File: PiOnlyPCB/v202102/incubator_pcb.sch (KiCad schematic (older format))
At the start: 34 parts, among them J1 Conn_01x04, J10 Conn_01x02, J11 Conn_01x02, J2 Conn_01x04, J3 Conn_01x04, J4 Conn_01x02, J5 Conn_01x02, J6 Conn_01x02, J7 Conn_01x02, J8 Conn_01x02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

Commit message: Partial version with GPIO expander too.
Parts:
- removed D1, D2: LED, Diode_SMD:D_0805_2012Metric_Pad1.15x1.40mm_HandSolder, symbol Device:LED
- removed J1, J2, J3: Conn_01x04, Connector_PinHeader_2.54mm:PinHeader_1x04_P2.54mm_Vertical, symbol Connector_Generic:Conn_01x04
- removed J10, J11, J4, J5, J6, J7, J8, J9: Conn_01x02, TerminalBlock_Phoenix:TerminalBlock_Phoenix_MKDS-1,5-2_1x02_P5.00mm_Horizontal, symbol Connector_Generic:Conn_01x02
- removed Q1, Q2, Q3, Q4: Q_NMOS_GDS, Package_TO_SOT_THT:TO-220-3_Vertical, symbol Device:Q_NMOS_GDS
- removed R10, R11, R12, R13, R14, R15, R2, R3, R4, R5, R6, R7, R8, R9: R_Small, Resistor_SMD:R_0805_2012Metric_Pad1.15x1.40mm_HandSolder, symbol Device:R_Small
- added J1: Conn_01x05, Connector_PinHeader_2.54mm:PinHeader_1x05_P2.54mm_Vertical, symbol Connector_Generic:Conn_01x05
- added J2: Conn_01x12_Female, v202102_OpenPlant:PWRCON_3M81-12, symbol Connector:Conn_01x12_Female
- added J3: Conn_01x05_Female, v202102_OpenPlant:PWRCON_3M81-5, symbol Connector:Conn_01x05_Female
- R1: footprint Resistor_SMD:R_0805_2012Metric_Pad1.15x1.40mm_HandSolder -> Resistor_SMD:R_0805_2012Metric_Pad1.20x1.40mm_HandSolder
- renumbered D3 to D1
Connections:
- net GND: now also J1.3 (Pin_3), J3.1 (Pin_1), J3.2 (Pin_2), J3.3 (Pin_3), J3.4 (Pin_4), J3.5 (Pin_5)
- net VCC3V3: now also J1.1 (Pin_1), J1.2 (Pin_2)
- net VCC5V: now also J1.4 (Pin_4), J1.5 (Pin_5)
- net IN5: now reaches U1.18 (GPIO24)
- net IN6: now reaches U1.19 (GPIO10_MOSI)
- net IN7: now reaches U1.21 (GPIO9_MISO)
- net IN8: now reaches U1.22 (GPIO25)
- net IN9: now reaches U1.23 (GPIO11_SCLK)
- net IN10: now reaches U1.24 (GPIO8_CE0)
- net IN11: now reaches U1.26 (GPIO7_CE1)
- net IN12: now reaches U1.27 (GPIO0_ID_SC)
- net GPIO12_PWM0 renamed IN1
- net GPIO13_PWM1 renamed IN2
- net GPIO22 renamed IN3
- net GPIO23 renamed IN4
- new net OUT1: J2.1 (Pin_1)
- new net OUT10: J2.10 (Pin_10)
- new net OUT11: J2.11 (Pin_11)
- new net OUT12: J2.12 (Pin_12)
- new net OUT2: J2.2 (Pin_2)
- new net OUT3: J2.3 (Pin_3)
- new net OUT4: J2.4 (Pin_4)
- new net OUT5: J2.5 (Pin_5)
- new net OUT6: J2.6 (Pin_6)
- new net OUT7: J2.7 (Pin_7)
- new net OUT8: J2.8 (Pin_8)
- new net OUT9: J2.9 (Pin_9)

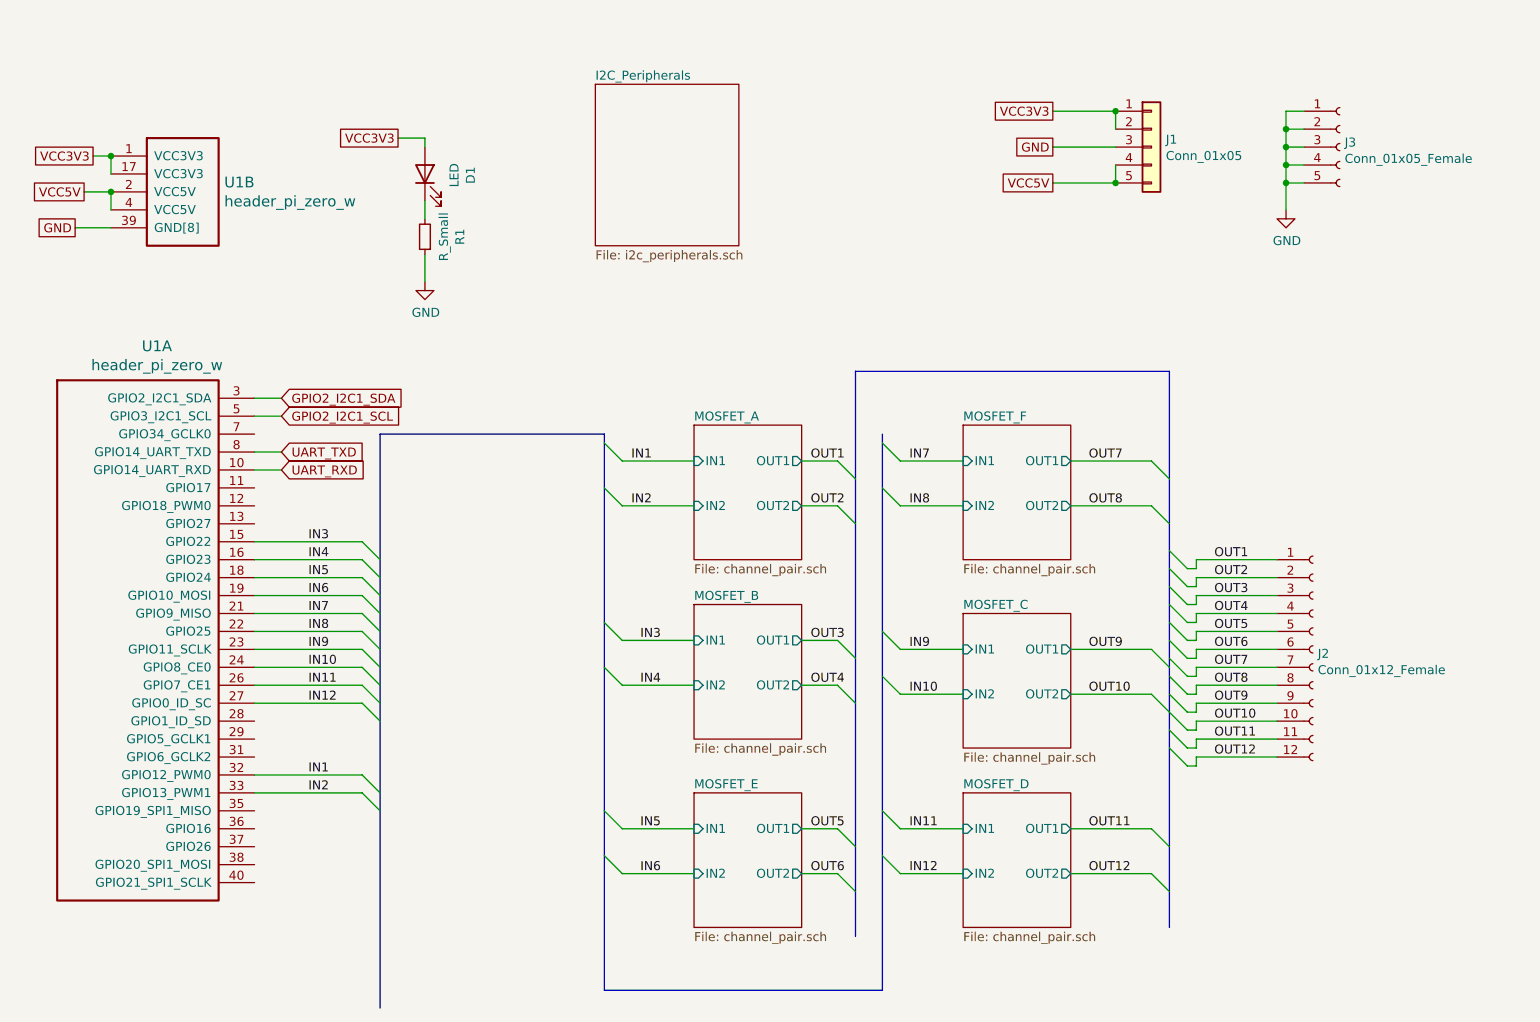
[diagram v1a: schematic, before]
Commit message: PCB Ready to order. Passed DRC.
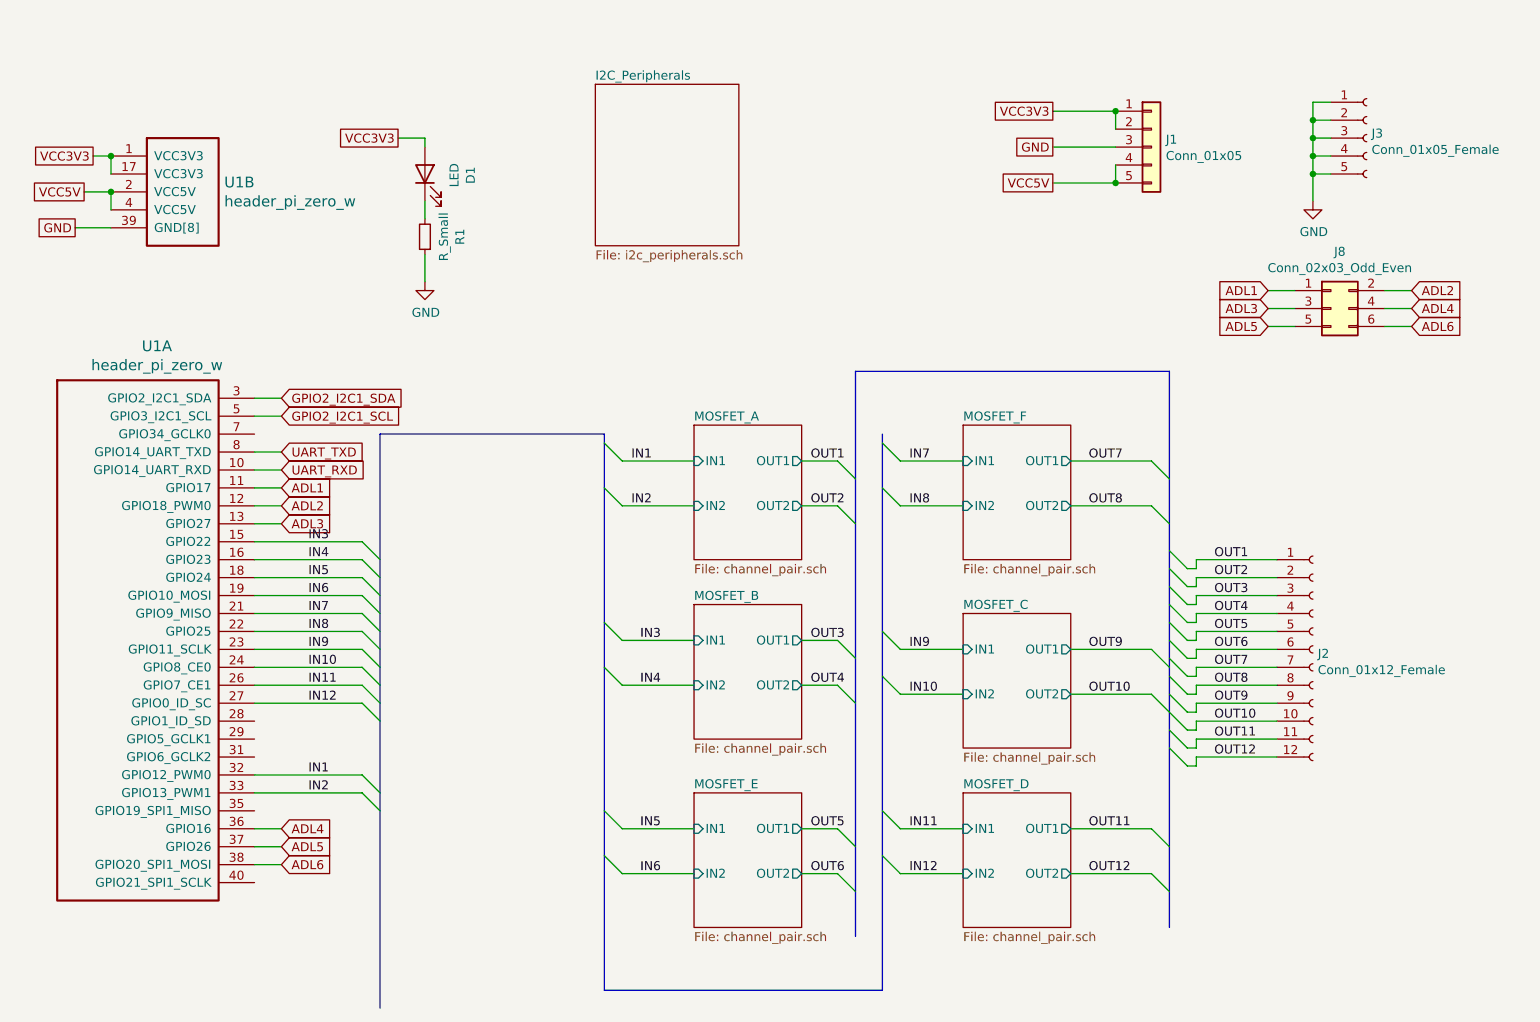
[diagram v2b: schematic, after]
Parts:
- added J8: Conn_02x03_Odd_Even, Connector_PinHeader_2.54mm:PinHeader_2x03_P2.54mm_Vertical, symbol Connector_Generic:Conn_02x03_Odd_Even
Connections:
- net ADL1: now reaches U1.11 (GPIO17)
- net ADL1: now also J8.1 (Pin_1)
- net ADL2: now reaches U1.12 (GPIO18_PWM0)
- net ADL2: now also J8.2 (Pin_2)
- net ADL3: now reaches U1.13 (GPIO27)
- net ADL3: now also J8.3 (Pin_3)
- net ADL4: now reaches U1.36 (GPIO16)
- net ADL4: now also J8.4 (Pin_4)
- net ADL5: now reaches U1.37 (GPIO26)
- net ADL5: now also J8.5 (Pin_5)
- net ADL6: now reaches U1.38 (GPIO20_SPI1_MOSI)
- net ADL6: now also J8.6 (Pin_6)
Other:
- moved on the sheet: J3
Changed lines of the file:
@@
 L Connector:Conn_01x05_Female J3
 U 1 1 60217AB3
-P 8100 1650
-F 0 "J3" H 8127 1676 50  0000 L CNN
-F 1 "Conn_01x05_Female" H 8127 1585 50  0000 L CNN
-F 2 "v202102_OpenPlant:PWRCON_3M81-5" H 8100 1650 50  0001 C CNN
-F 3 "~" H 8100 1650 50  0001 C CNN
-	1    8100 1650
+P 8250 1600
+F 0 "J3" H 8277 1626 50  0000 L CNN
+F 1 "Conn_01x05_Female" H 8277 1535 50  0000 L CNN
+F 2 "v202102_OpenPlant:PWRCON_3M81-5" H 8250 1600 50  0001 C CNN
+F 3 "~" H 8250 1600 50  0001 C CNN
+	1    8250 1600
 	1    0    0    -1
 $EndComp
@@
 L power:GND #PWR02
 U 1 1 60217B8E
-P 7800 2000
-F 0 "#PWR02" H 7800 1750 50  0001 C CNN
-F 1 "GND" H 7805 1827 50  0000 C CNN
-F 2 "" H 7800 2000 50  0001 C CNN
-F 3 "" H 7800 2000 50  0001 C CNN
-	1    7800 2000
+P 7950 1950
+F 0 "#PWR02" H 7950 1700 50  0001 C CNN
+F 1 "GND" H 7955 1777 50  0000 C CNN
+F 2 "" H 7950 1950 50  0001 C CNN
+F 3 "" H 7950 1950 50  0001 C CNN
+	1    7950 1950
 	1    0    0    -1
 $EndComp
 Wire Wire Line
-	7800 2000 7800 1850
-Wire Wire Line
-	7800 1850 7900 1850
-Wire Wire Line
-	7800 1850 7800 1750
-Wire Wire Line
-	7800 1450 7900 1450
-Connection ~ 7800 1850
-Wire Wire Line
-	7800 1550 7900 1550
-Connection ~ 7800 1550
-Wire Wire Line
-	7800 1550 7800 1450
-Wire Wire Line
-	7900 1650 7800 1650
-Connection ~ 7800 1650
-Wire Wire Line
-	7800 1650 7800 1550
-Wire Wire Line
-	7800 1750 7900 1750
-Connection ~ 7800 1750
-Wire Wire Line
-	7800 1750 7800 1650
+	7950 1950 7950 1800
+Wire Wire Line
+	7950 1800 8050 1800
+Wire Wire Line
+	7950 1800 7950 1700
+Wire Wire Line
+	7950 1400 8050 1400
+Connection ~ 7950 1800
+Wire Wire Line
+	7950 1500 8050 1500
+Connection ~ 7950 1500
+Wire Wire Line
+	7950 1500 7950 1400
+Wire Wire Line
+	8050 1600 7950 1600
+Connection ~ 7950 1600
+Wire Wire Line
+	7950 1600 7950 1500
+Wire Wire Line
+	7950 1700 8050 1700
+Connection ~ 7950 1700
+Wire Wire Line
+	7950 1700 7950 1600
 $Sheet
 S 4500 3200 600  750
@@
 Wire Wire Line
 	2050 5150 2650 5150
-Wire Wire Line
-	2050 5250 2650 5250
 Text Label 2350 5150 0    50   ~ 0
 IN1
@@
 	6850 1850 6850 1750
 Connection ~ 6850 1850
+Text GLabel 2200 3550 2    50   Input ~ 0
+ADL1
+Text GLabel 2200 3650 2    50   Input ~ 0
+ADL2
+Text GLabel 2200 3750 2    50   Input ~ 0
+ADL3
+Text GLabel 2200 5450 2    50   Input ~ 0
+ADL4
+Text GLabel 2200 5550 2    50   Input ~ 0
+ADL5
+Text GLabel 2200 5650 2    50   Input ~ 0
+ADL6
+Wire Wire Line
+	2050 3550 2200 3550
+Wire Wire Line
+	2050 3650 2200 3650
+Wire Wire Line
+	2050 3750 2200 3750
+Wire Wire Line
+	2050 5450 2200 5450
+Wire Wire Line
+	2050 5550 2200 5550
+Wire Wire Line
+	2050 5650 2200 5650
+Text GLabel 7700 2450 0    50   Input ~ 0
+ADL1
+Text GLabel 8500 2450 2    50   Input ~ 0
+ADL2
+Text GLabel 7700 2550 0    50   Input ~ 0
+ADL3
+Wire Wire Line
+	7850 2450 7700 2450
+Wire Wire Line
+	8350 2450 8500 2450
+Wire Wire Line
+	7850 2550 7700 2550
+Text GLabel 8500 2550 2    50   Input ~ 0
+ADL4
+Text GLabel 7700 2650 0    50   Input ~ 0
+ADL5
+Text GLabel 8500 2650 2    50   Input ~ 0
+ADL6
+Wire Wire Line
+	8350 2550 8500 2550
+Wire Wire Line
+	7850 2650 7700 2650
+Wire Wire Line
+	8350 2650 8500 2650
+$Comp
+L Connector_Generic:Conn_02x03_Odd_Even J8
+U 1 1 60439022
+P 8050 2550
+F 0 "J8" H 8100 2867 50  0000 C CNN
+F 1 "Conn_02x03_Odd_Even" H 8100 2776 50  0000 C CNN
+F 2 "Connector_PinHeader_2.54mm:PinHeader_2x03_P2.54mm_Vertical" H 8050 2550 50  0001 C CNN
+F 3 "~" H 8050 2550 50  0001 C CNN
+	1    8050 2550
+	1    0    0    -1
+$EndComp
+Wire Wire Line
+	2050 5250 2650 5250
 Wire Bus Line
 	5400 2900 5400 6050
